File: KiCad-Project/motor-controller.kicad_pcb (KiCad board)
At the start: 2 copper layers, 160 x 100 mm, 85 parts, among them J101 24V, J102 12V, J103 GND, J201 Encoder, J202 GPIO, J203 UPDI, J204 Bus, J401 MOTOR, J402 ~MOTOR, Q401 DMTH6002LPS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

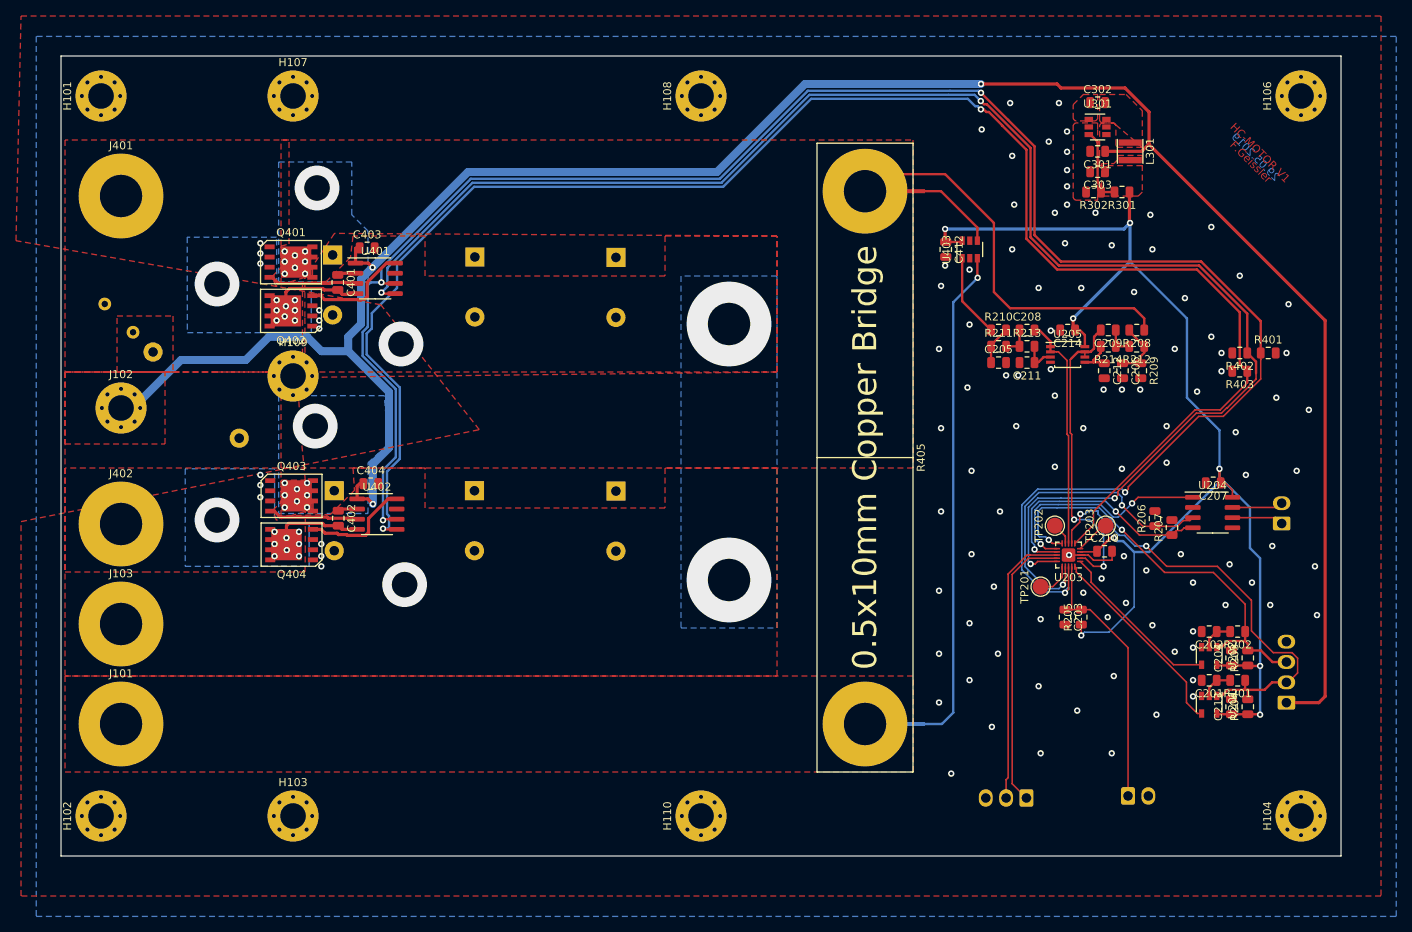
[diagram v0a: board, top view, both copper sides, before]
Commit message: Single layer Board
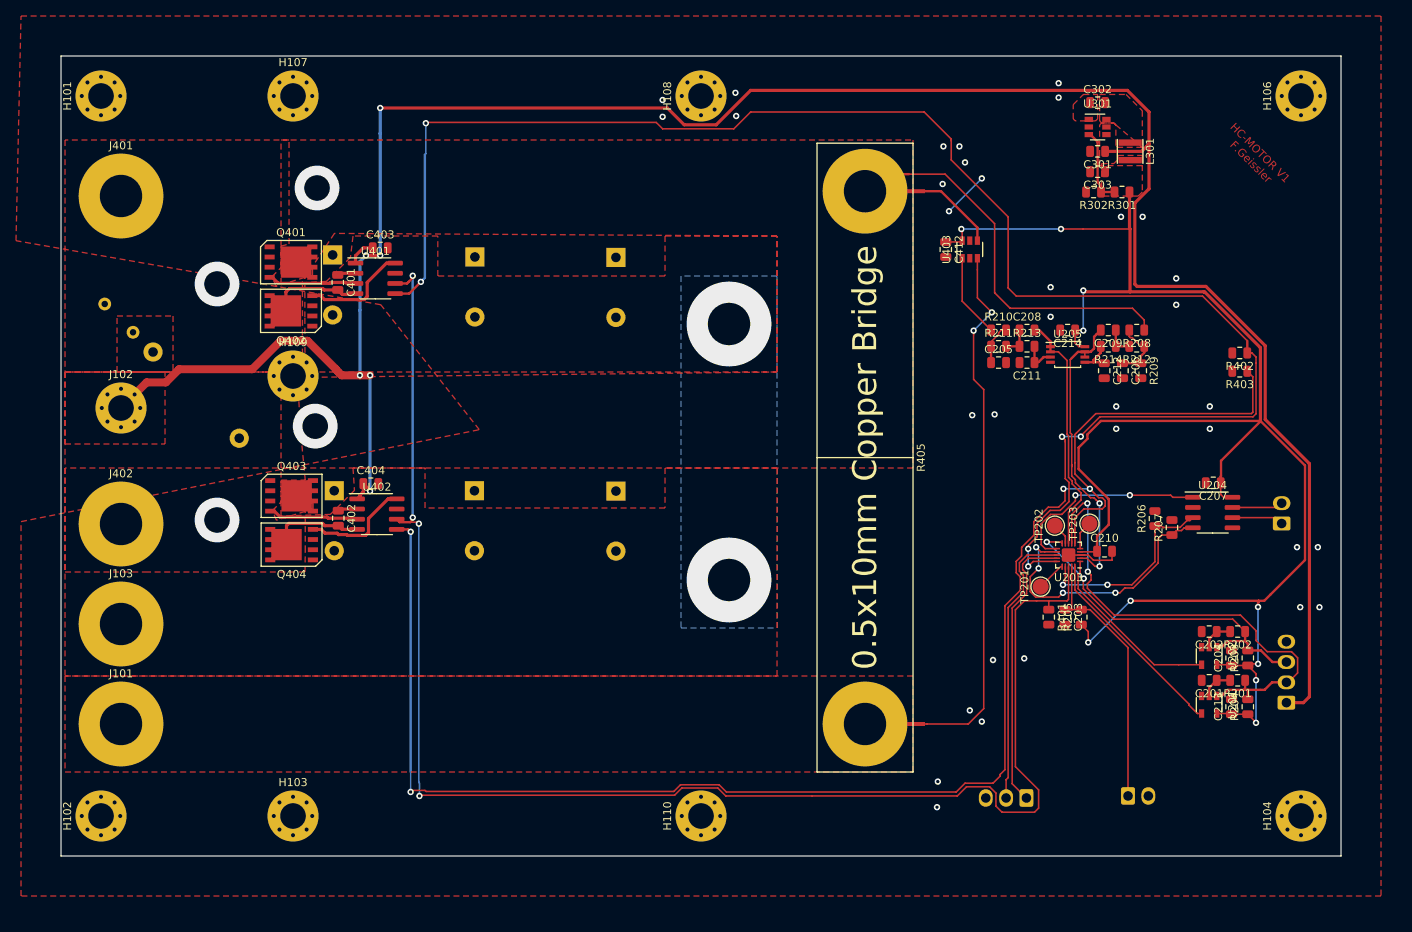
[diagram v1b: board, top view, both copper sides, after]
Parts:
- moved R401 42.9 mm to (188.5, 120.1), turned to 270 degrees
- moved TP203 2.05 mm to (193.5, 108.5)
- moved C403 1.63 mm to (104.9, 74.0)
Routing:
- net /Controller/BR_EN: track 240.5 -> 190.3 mm, vias 5 -> 4
- net +3V3: track 168.8 -> 214.9 mm, vias 8 -> 10
- net /Controller/TX_EN: track 40.5 -> 24.9 mm
- net +12V: track 276.5 -> 290.8 mm, vias 3 -> 6
- net /Controller/PWM: track 194.1 -> 205.1 mm, vias 4 -> 6
- net /Controller/~PWM: track 211.1 -> 200.9 mm, vias 2 -> 4
- net /Controller/ROT_B: track 52.7 -> 44.0 mm
- net /Controller/ROT_A: track 57.4 -> 63.7 mm
- net GND: track 7.36 -> 13.2 mm, vias 109 -> 36
- net Net-(R405-Pad2): track 63.9 -> 68.6 mm, vias 1 -> 2
- net /Controller/TXD: track 30.8 -> 34.9 mm, vias 2 -> 4
- net /Controller/RXD: track 28.7 -> 25.7 mm
- net /Controller/ROT_B_EDGE: track 21.3 -> 22.9 mm
- net /Controller/ADC_VOLTAGE: track 38.9 -> 37.6 mm
- net /Controller/ADC_CURRENT: track 29.4 -> 30.7 mm
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- removed copper zone on B.Cu, net /Controller/VRAIL
- removed copper zone on B.Cu, net Net-(C401-Pad2)
- removed copper zone on B.Cu, net Net-(C402-Pad2)
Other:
- board text removed: "29.05.2019"

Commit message: Battry Protection added
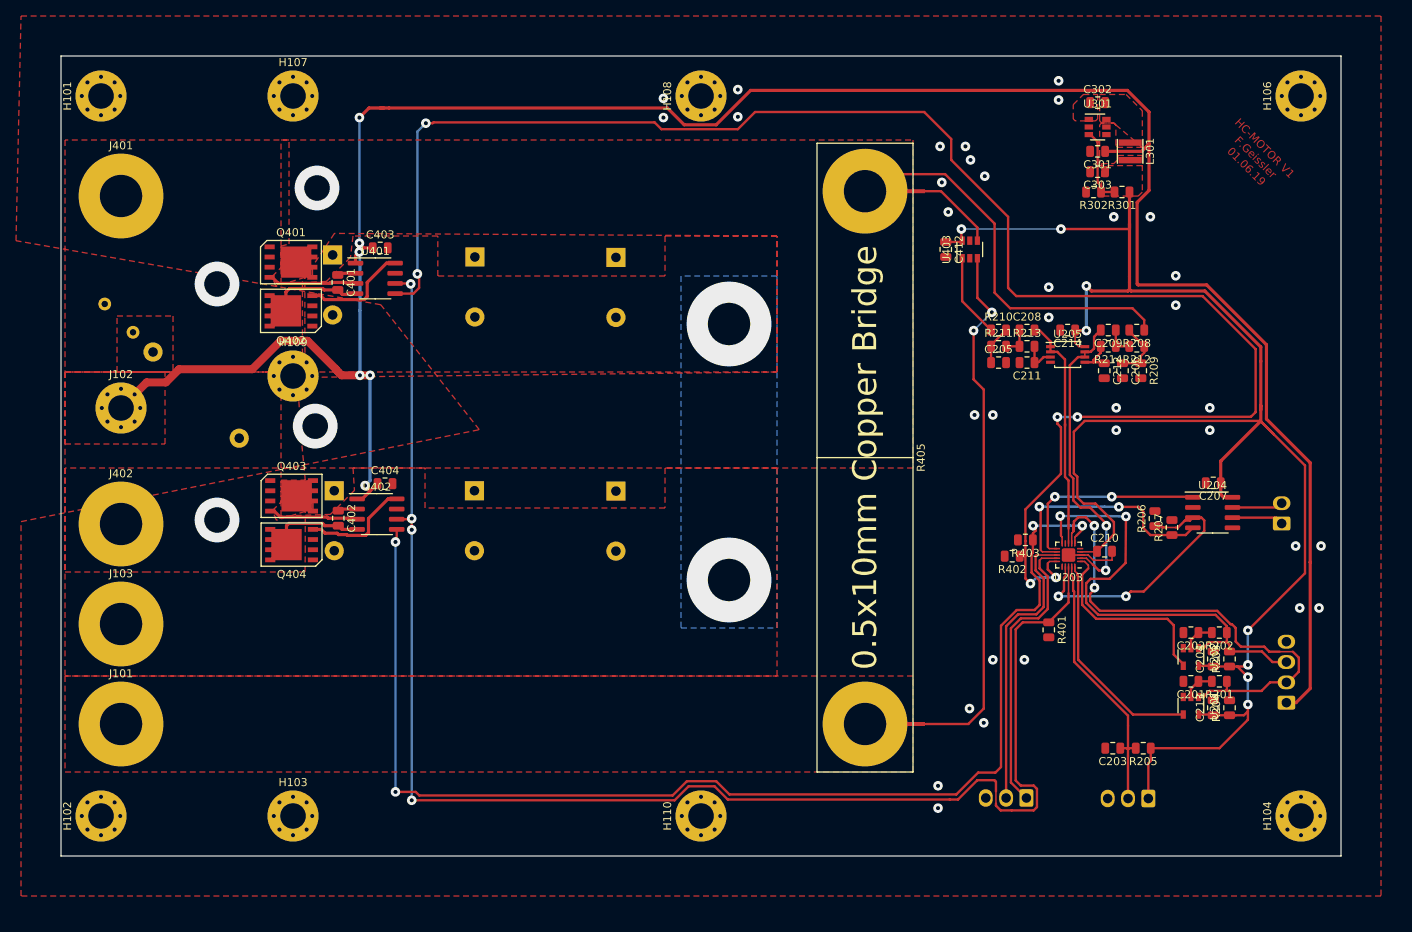
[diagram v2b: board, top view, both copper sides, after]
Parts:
- removed TP201: ROT_DIR, TestPoint:TestPoint_Pad_D2.0mm
- removed TP202: CLK_OUT, TestPoint:TestPoint_Pad_D2.0mm
- removed TP203: ROT_CNT, TestPoint:TestPoint_Pad_D2.0mm
- J203: footprint Connector_Molex:Molex_KK-254_AE-6410-02A_1x02_P2.54mm_Vertical -> Connector_Molex:Molex_KK-254_AE-6410-03A_1x03_P2.54mm_Vertical
- moved R402 38.1 mm to (183.9, 112.5)
- moved R403 34.1 mm to (185.5, 110.5)
- moved R205 18.1 mm to (200.3, 136.5), turned to 180 degrees
- moved C203 17.4 mm to (196.5, 136.5), turned to 180 degrees
- moved J203 2.56 mm to (200.9, 142.8), turned to 180 degrees
- moved C201 2.29 mm to (206.2, 128.2)
- moved C204 2.29 mm to (209.0, 125.4)
- moved R201 2.29 mm to (209.8, 128.2)
- moved R203 2.29 mm to (211.1, 125.4)
- moved U201 2.29 mm to (206.2, 131.2)
- moved C202 2.29 mm to (206.2, 122.1)
- moved R202 2.29 mm to (209.8, 122.1)
- moved U202 2.29 mm to (206.2, 125.1)
- moved C213 2.29 mm to (209.0, 131.5)
- moved R204 2.29 mm to (211.1, 131.5)
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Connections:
- J203 pad 1: /Controller/~RESET -> +3V3
- J203 pad 2: GND -> /Controller/~RESET
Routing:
- net /Controller/~PWM: track 200.9 -> 154.8 mm
- net /Controller/ROT_B: track 44.0 -> 59.6 mm
- net +3V3: track 214.9 -> 225.0 mm, vias 10 -> 8
- net /Controller/TX_EN: track 24.9 -> 33.9 mm
- net /Controller/PWM: track 205.1 -> 212.1 mm
- net GND: track 13.2 -> 7.36 mm
- net /Controller/TXD: track 34.9 -> 29.8 mm, vias 4 -> 2
- net Net-(TP201-Pad1): track 3.72 -> 0.00 mm
- net Net-(TP203-Pad1): track 3.60 -> 0.00 mm
- net Net-(TP202-Pad1): track 2.76 -> 0.00 mm
- net /Controller/ROT_A_EDGE: track 25.2 -> 27.8 mm
- net /Controller/ROT_B_EDGE: track 22.9 -> 24.6 mm
- net /Controller/ADC_VOLTAGE: track 37.6 -> 39.1 mm
- net +12V: track 290.8 -> 292.1 mm
- net /Controller/ROT_A: track 63.7 -> 64.9 mm
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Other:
- net class Default: clearance 0.2 -> 0.3; via_dia 0.8 -> 1.2; via_drill 0.4 -> 0.5
- rule trace_clearance: 0.2 -> 0.3
- board text added: "HC-MOTOR V1 F.Geissler 01.06.19"
- board text removed: "HC-MOTOR V1 F.Geissler"
